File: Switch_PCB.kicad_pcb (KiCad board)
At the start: 2 copper layers, 213 x 96.6 mm, 60 parts, among them J1 Black, J10 Black, J11 Red, J12 Conn_01x02, J13 Conn_01x03, J14 Conn_01x03, J15 Conn_01x03, J16 Conn_01x03, J17 Jack 2.1mm, J18 Jack 2.1mm, J19 Black, J2 Red, J20 Red, J21 Black, J22 Red, J23 Black, J24 Red, J25 Black, J26 Red, J27 Black, J28 Red, J29 Black, J3 Black, J30 Red, J31 Black, J32 Red, J33 Black, J34 Red, J4 Red, J5 Black, J6 Red, J7 Black, J8 Red, J9 Red, SW1 Switch On-Off-On, SW2 Switch On-Off-On, SW3 Switch On-Off-On, SW4 Switch On-Off-On

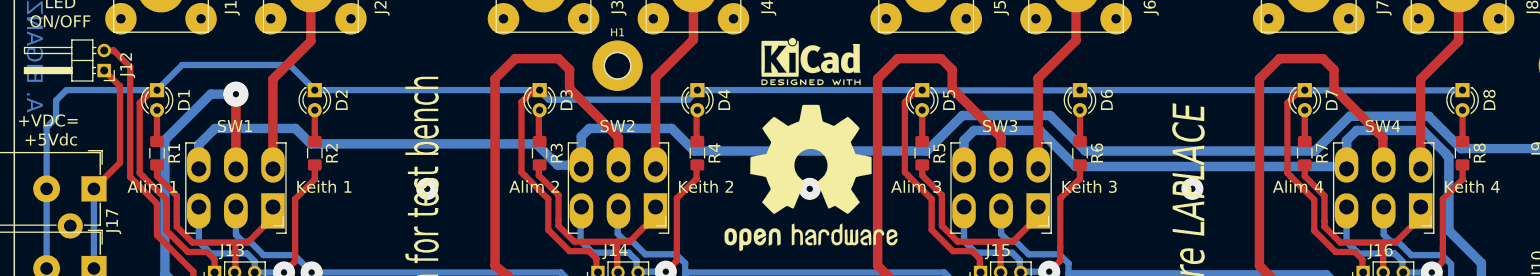
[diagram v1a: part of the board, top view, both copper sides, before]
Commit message: Update local inter footprint SW_TME_1MD3T1B1M1QE_DPDT_Straight.kicad_mod, change for oblong hole. Add packages3D in kicad_local_mod folder.
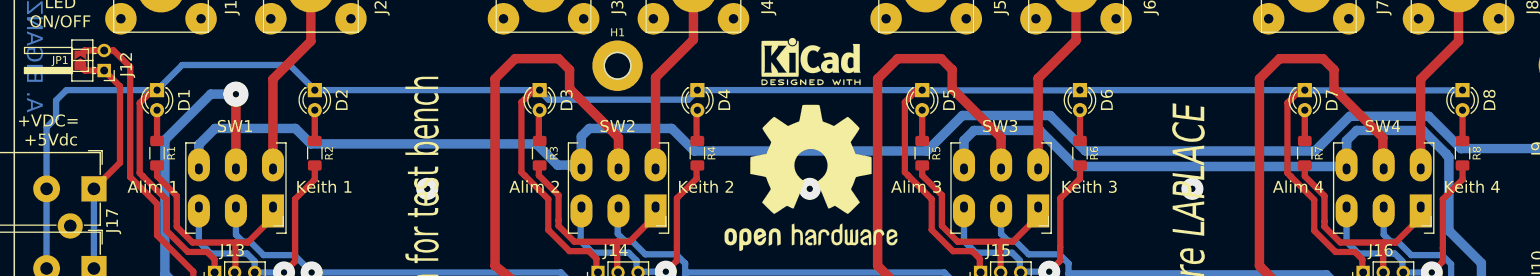
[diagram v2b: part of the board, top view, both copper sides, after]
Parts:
- added JP1: SolderJumper_2_Open, Jumper:SolderJumper-2_P1.3mm_Open_TrianglePad1.0x1.5mm, F.Cu at (45.7, 60.3)
- J1, J10, J27, J29, J3, J31, J33, J5, J7: footprint ArnauldDev_Connector_Banana:SCHUTZINGER_SWEB8094AU-SW_4mm_Horizontal_Black -> Local_Connector_Banana:SCHUTZINGER_SWEB8094AU-SW_4mm_Horizontal_Black
- J11, J2, J28, J30, J32, J34, J4, J6, J8, J9: footprint ArnauldDev_Connector_Banana:SCHUTZINGER_SWEB8094AU-RT_4mm_Horizontal_Red -> Local_Connector_Banana:SCHUTZINGER_SWEB8094AU-RT_4mm_Horizontal_Red
- J17, J18: footprint ArnauldDev_Connector_BarrelJack:BarrelJack_FC681465P_Pin3_Horizontal -> Local_Connector_BarrelJack:BarrelJack_FC681465P_Pin3_Horizontal
- J19, J21, J23, J25: footprint ArnauldDev_Connector_Banana:STAUBLI_66.9032-21_XELA-4_4mm_Vertical_Black -> Local_Connector_Banana:STAUBLI_66.9032-21_XELA-4_4mm_Vertical_Black
- J20, J22, J24, J26: footprint ArnauldDev_Connector_Banana:STAUBLI_66.9032-22_XELA-4_4mm_Vertical_Red -> Local_Connector_Banana:STAUBLI_66.9032-22_XELA-4_4mm_Vertical_Red
- R1, R2, R3, R4, R5, R6, R7, R8: footprint Resistor_SMD:R_1206_3216Metric_Pad1.42x1.75mm_HandSolder -> Resistor_SMD:R_1206_3216Metric_Pad1.30x1.75mm_HandSolder
- SW1, SW2, SW3, SW4: footprint ArnauldDev_Button_Switch_THT:SW_TME_1MD3T1B1M1QE_DPDT_Straight -> Local_Button_Switch_THT:SW_TME_1MD3T1B1M1QE_DPDT_Straight
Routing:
- net +VDC: track 27.3 -> 30.5 mm
- net +5VD: track 265.0 -> 267.7 mm

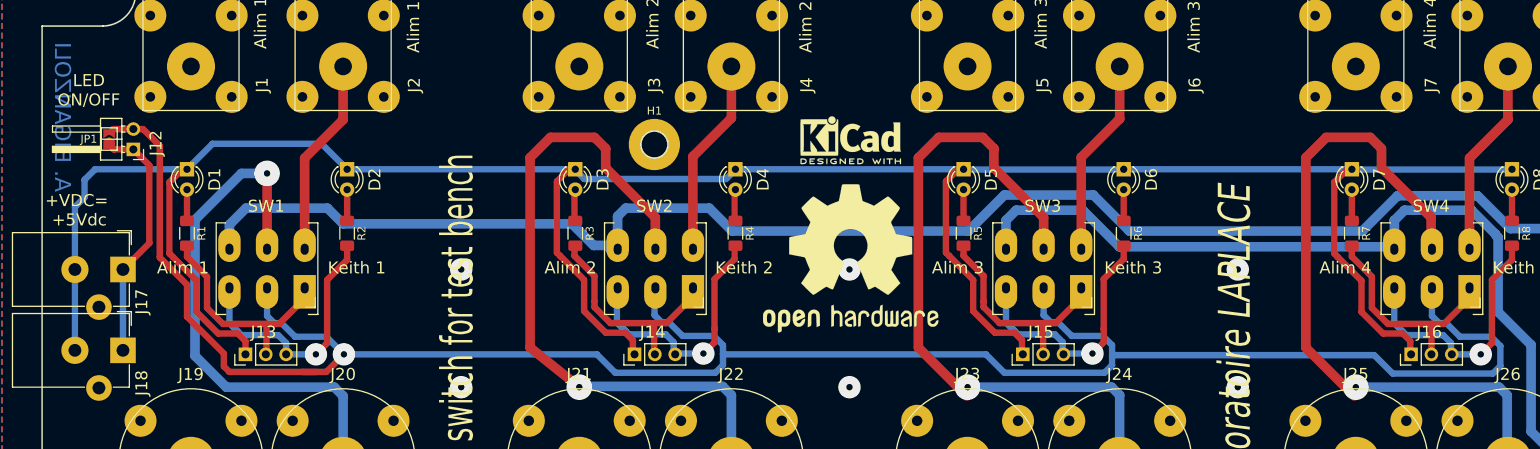
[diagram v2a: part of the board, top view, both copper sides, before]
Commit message: Change 3dshapes file name from (model ${ARNAULDDEV_SYS3DMOD}/ArnauldDev_ to (model ${KIPRJMOD}/kicad_local_mod/packages3d/
kicad_local_mod/packages3d/ArnauldDev_Button_Switch_THT.3dshapes/SW_DPDT_11.43x12.70mm_W4.83mm_P4.70mm_Straight.step
kicad_local_mod/packages3d/ArnauldDev_Button_Switch_THT.3dshapes/SW_DPDT_11.43x12.70mm_W4.83mm_P4.70mm_Straight.wrl
kicad_local_mod/packages3d/ArnauldDev_Connector_Banana.3dshapes/SCHUTZINGER_SWEB8094AU-SW_4mm_Horizontal_Black.step
kicad_local_mod/packages3d/ArnauldDev_Connector_Banana.3dshapes/SCHUTZINGER_SWEB8094AU-SW_4mm_Horizontal_Red.step
kicad_local_mod/packages3d/ArnauldDev_Connector_Banana.3dshapes/STAUBLI_66.9032-21_XELA-4_4mm_Vertical_Black.step
kicad_local_mod/packages3d/ArnauldDev_Connector_Banana.3dshapes/STAUBLI_66.9032-21_XELA-4_4mm_Vertical_Black.wrl
kicad_local_mod/packages3d/ArnauldDev_Connector_Banana.3dshapes/STAUBLI_66.9032-22_XELA-4_4mm_Vertical_Red.step
kicad_local_mod/packages3d/ArnauldDev_Connector_Banana.3dshapes/STAUBLI_66.9032-22_XELA-4_4mm_Vertical_Red.wrl
kicad_local_mod/packages3d/ArnauldDev_Connector_BarrelJack.3dshapes/DC_Power_Jack_5.5x2.1mm.step
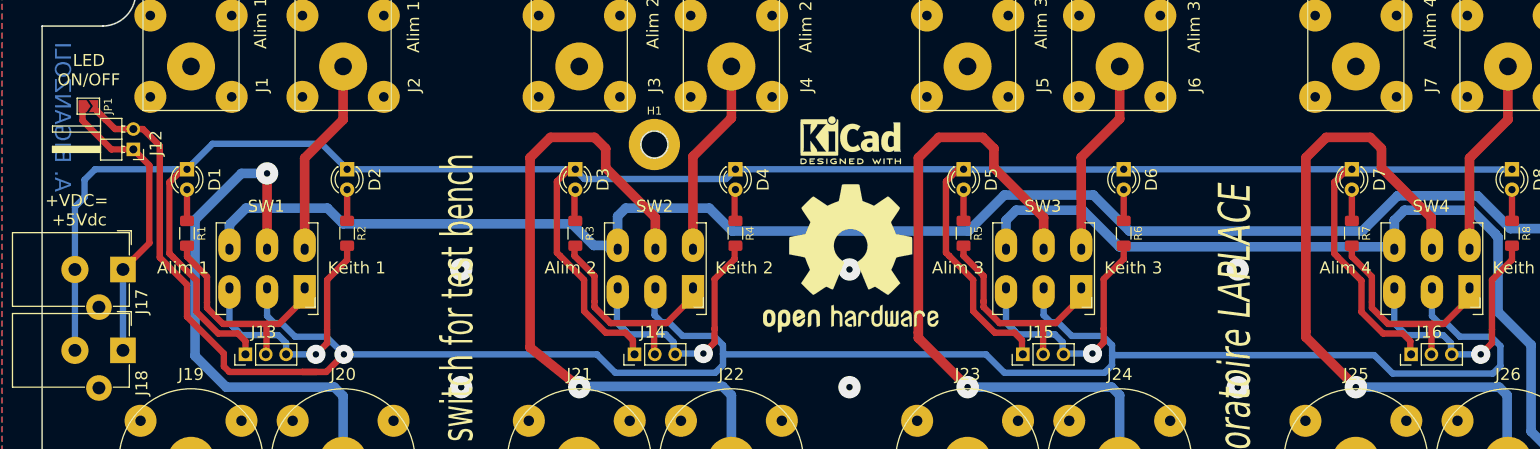
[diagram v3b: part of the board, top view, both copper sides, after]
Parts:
- moved JP1 4.86 mm to (43.1, 56.2), turned to 0 degrees
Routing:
- net +VDC: track 30.5 -> 36.9 mm
- net +5VD: track 267.7 -> 272.1 mm
- net RELAY_V3+: track 86.0 -> 84.9 mm
- net RELAY_V4+: track 85.9 -> 84.9 mm

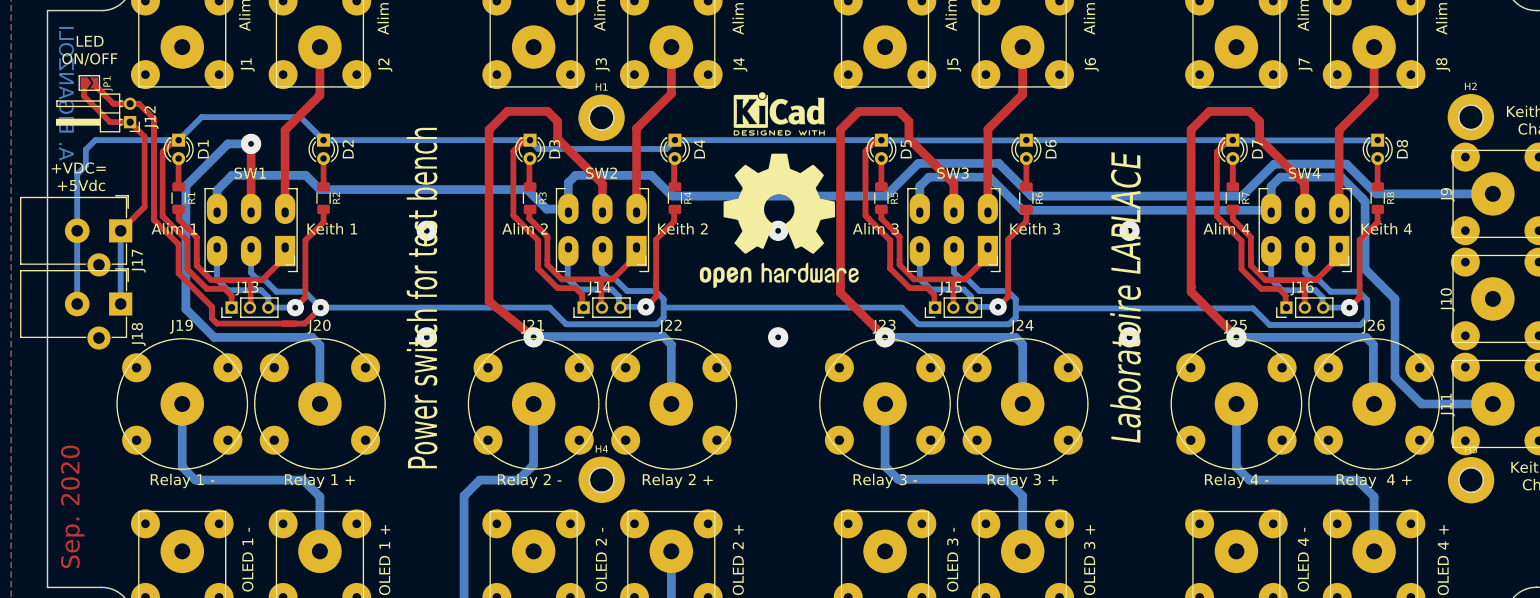
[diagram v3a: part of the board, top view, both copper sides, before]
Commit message: Update path for 3D modeles to packages3d Add fiducial marks in pcb
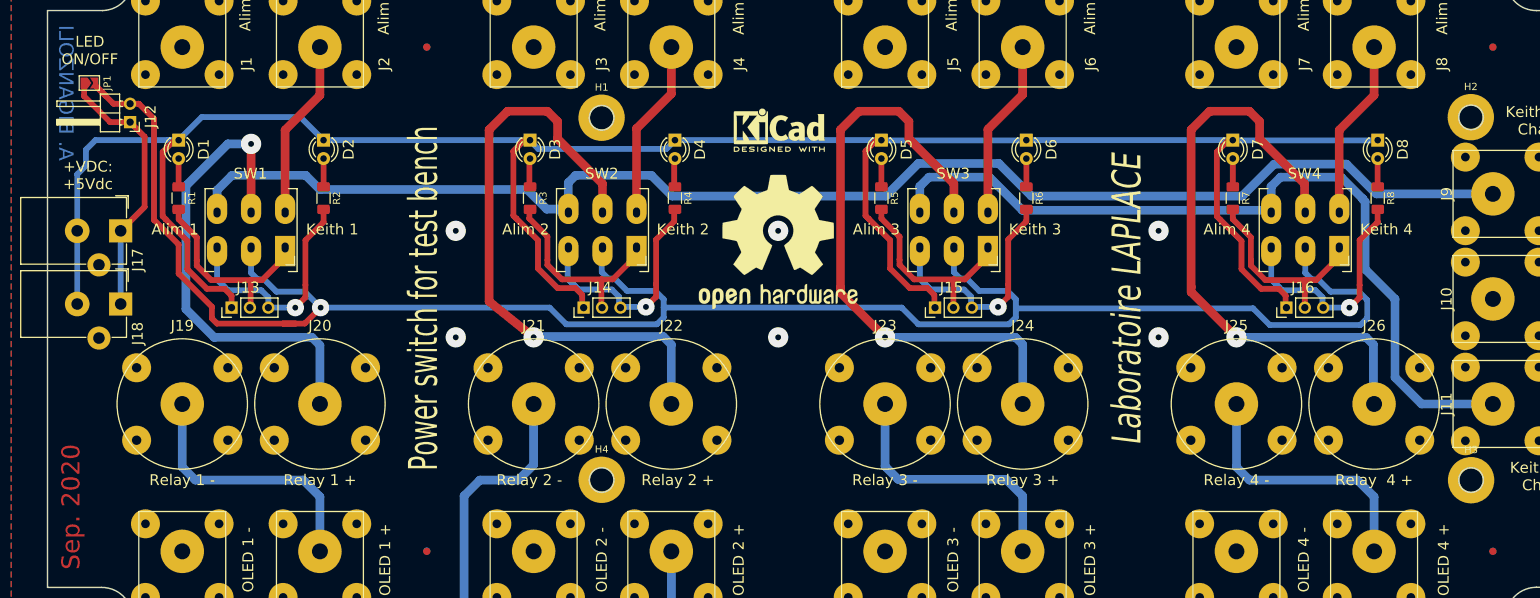
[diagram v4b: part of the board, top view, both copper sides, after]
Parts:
- added REF**: Fiducial_1mm_Mask3mm, Fiducial:Fiducial_1mm_Mask3mm, B.Cu at (89.7, 120.8)
- added REF**: Fiducial_1mm_Mask3mm, Fiducial:Fiducial_1mm_Mask3mm, B.Cu at (236.8, 120.8)
- added REF**: Fiducial_1mm_Mask3mm, Fiducial:Fiducial_1mm_Mask3mm, B.Cu at (236.8, 51.2)
- added REF**: Fiducial_1mm_Mask3mm, Fiducial:Fiducial_1mm_Mask3mm, B.Cu at (89.7, 51.2)
- added REF**: Fiducial_1mm_Mask3mm, Fiducial:Fiducial_1mm_Mask3mm, F.Cu at (236.8, 120.8)
- added REF**: Fiducial_1mm_Mask3mm, Fiducial:Fiducial_1mm_Mask3mm, F.Cu at (89.7, 120.8)
- added REF**: Fiducial_1mm_Mask3mm, Fiducial:Fiducial_1mm_Mask3mm, F.Cu at (89.7, 51.2)
- added REF**: Fiducial_1mm_Mask3mm, Fiducial:Fiducial_1mm_Mask3mm, F.Cu at (236.8, 51.2)
- moved REF** 2.92 mm to (138.2, 78.1)
- moved ? 2.25 mm to (138.3, 62.7)
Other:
- board text added: "+VDC: +5Vdc"
- board text removed: "+VDC= +5Vdc"

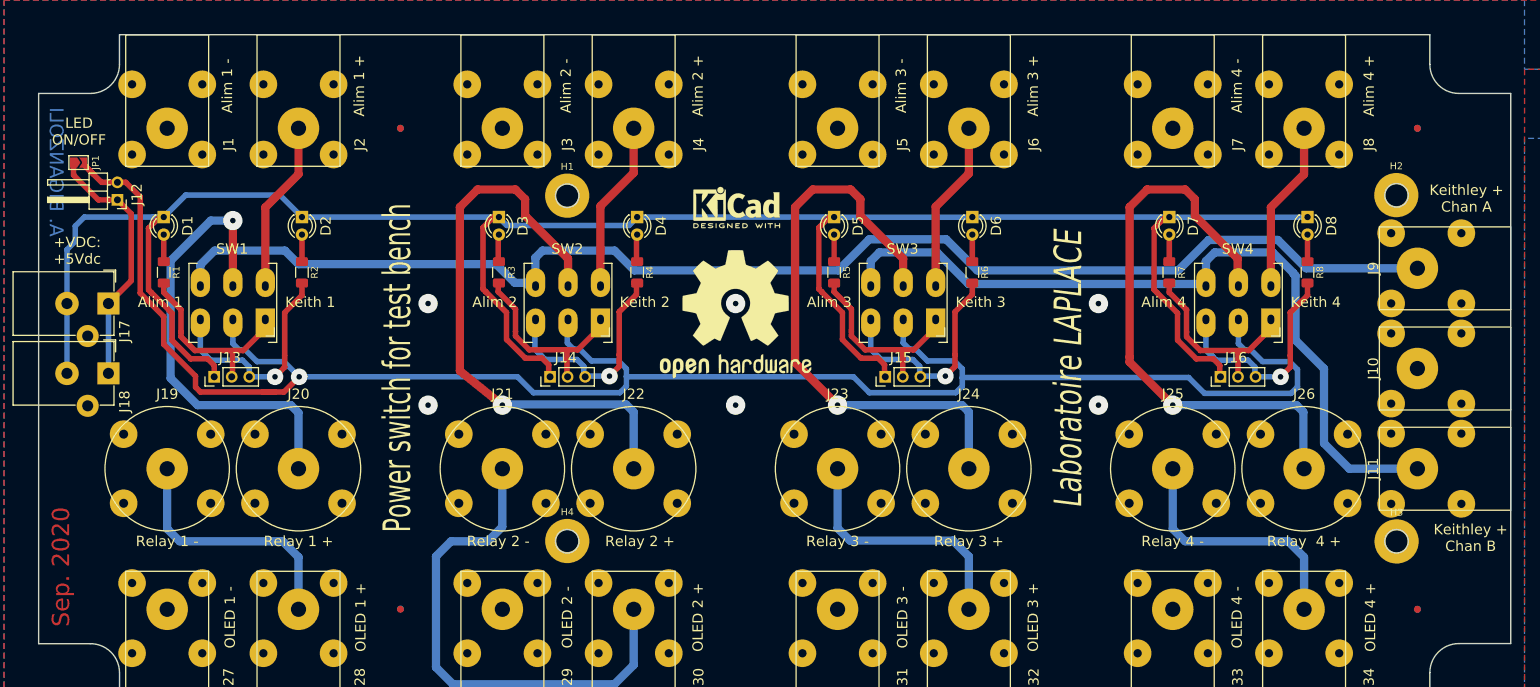
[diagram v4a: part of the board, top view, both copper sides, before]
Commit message: Update project Add layers number
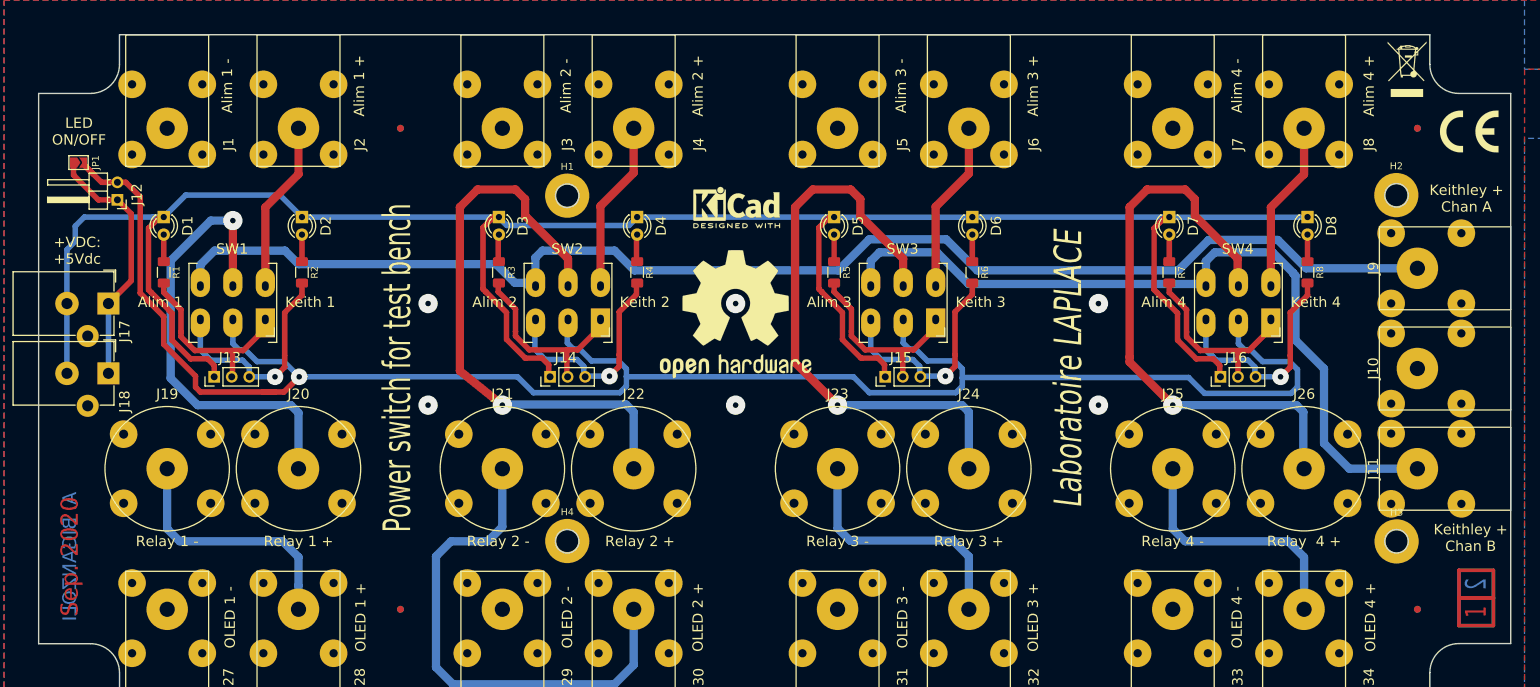
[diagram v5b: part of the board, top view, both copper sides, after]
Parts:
- added REF**: WEEE-Logo_5.6x8mm_SilkScreen, Symbol:WEEE-Logo_5.6x8mm_SilkScreen, F.Cu at (235.3, 42.7)
- added REF**: CE-Logo_8.5x6mm_SilkScreen, Symbol:CE-Logo_8.5x6mm_SilkScreen, F.Cu at (244.3, 51.7)
- added Ref**: L, Local_Layer_ID:L, B.Cu at (245.3, 117.2)
- added Ref**: L, Local_Layer_ID:L, B.Cu at (245.3, 121.2)
- added Ref**: L, Local_Layer_ID:L, F.Cu at (245.3, 117.2)
- added Ref**: L, Local_Layer_ID:L, F.Cu at (245.3, 121.2)
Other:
- board text added: "1"
- board text added: "2"
- board text added: "BOTTOM GNDPWR"
- board text added: "TOP GNDPWR"
